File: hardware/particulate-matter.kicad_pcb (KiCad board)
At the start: 2 copper layers, 70 x 40 mm, 30 parts, among them P1 CON-SENSOR2, P2 BOOT, P3 DEBUG, U1 XMC1XXX48, U2 DRILL, U3 DRILL, U4 DRILL, U5 DRILL, U6 PMS7003, X1 16MHz

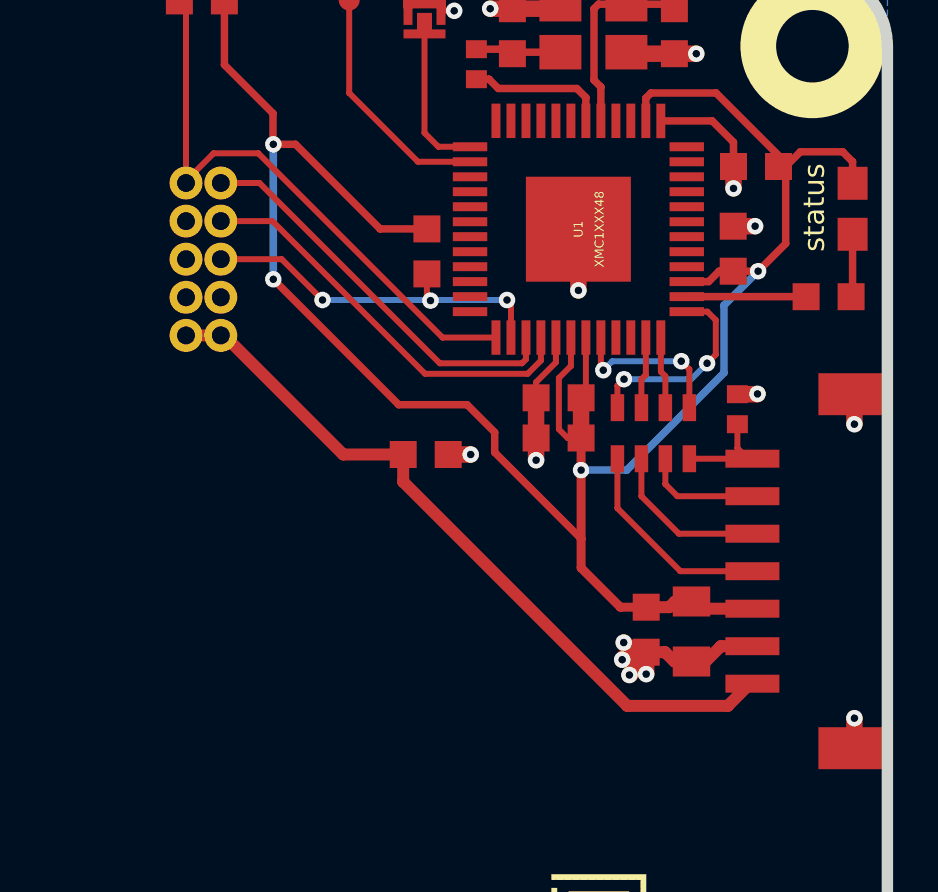
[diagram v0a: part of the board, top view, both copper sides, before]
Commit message: Add resistors for TX/RX and another capacitor for the PMS Sensor
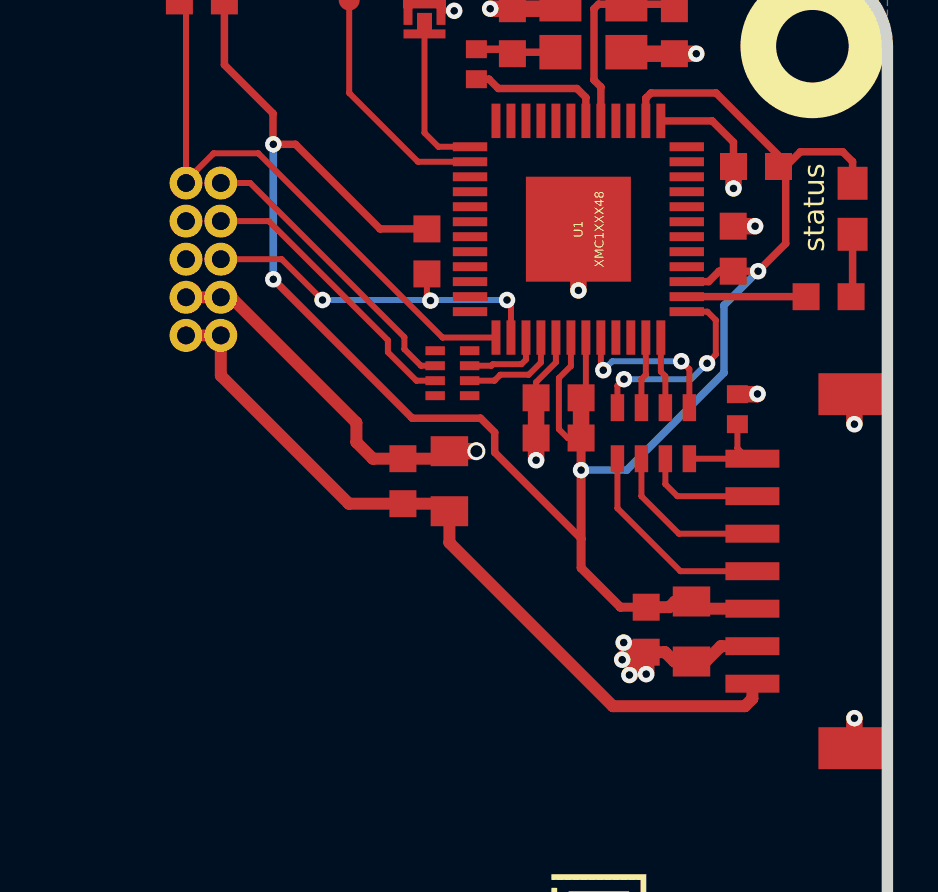
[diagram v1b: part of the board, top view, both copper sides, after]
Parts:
- added C11: 10uF, kicad-libraries:C0805, F.Cu at (156.2, 82.0)
- added RP2: 100, 4X0402, F.Cu at (156.3, 78.4)
- C1: value 1uF -> 10uF
- moved C10 1.17 mm to (154.7, 82.0), turned to 90 degrees
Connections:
- U6 pad 7: PMS_RX -> Net-(RP2-Pad3)
- U6 pad 9: PMS_TX -> Net-(RP2-Pad2)
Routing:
- net GND: track 29.2 -> 40.9 mm
- net PMS_TX: track 13.4 -> 2.70 mm
- net PMS_RX: track 13.7 -> 3.46 mm
- net Net-(RP2-Pad2): track 0.00 -> 9.90 mm
- net Net-(RP2-Pad3): track 0.00 -> 9.58 mm
- net +5V: track 24.8 -> 26.2 mm

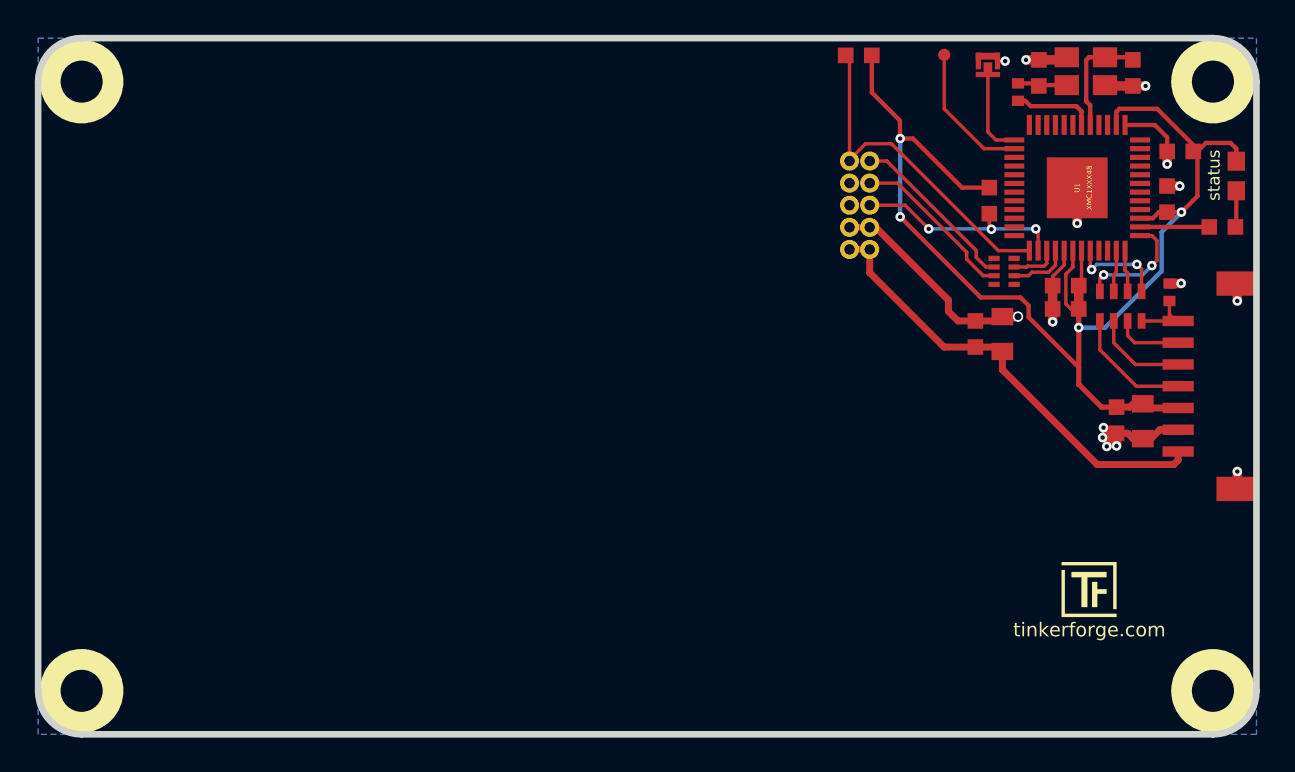
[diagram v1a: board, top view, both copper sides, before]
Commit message: add fiducial marks
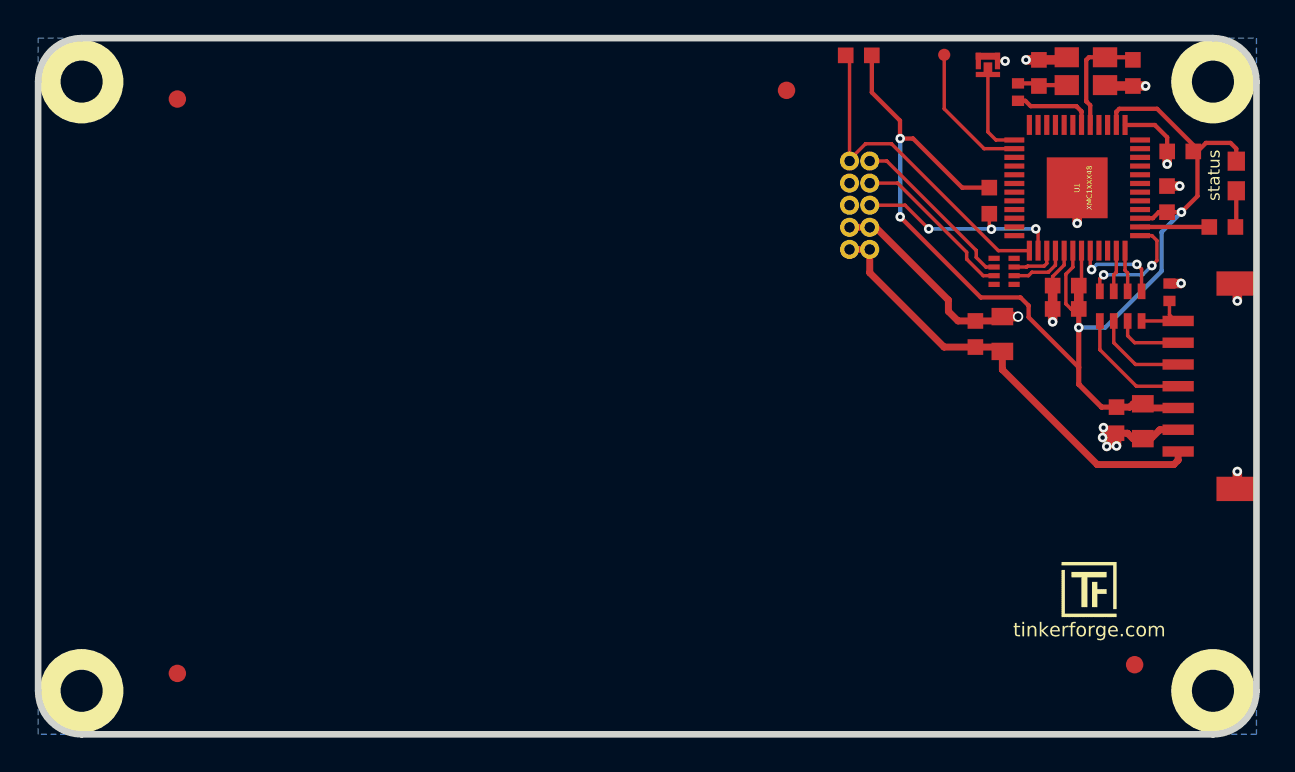
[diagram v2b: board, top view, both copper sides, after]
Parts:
- added Fiducial_Mark: VAL**, kicad-libraries:Fiducial_Mark, F.Cu at (163.8, 101.0)
- added Fiducial_Mark: VAL**, kicad-libraries:Fiducial_Mark, F.Cu at (108.8, 101.5)
- added Fiducial_Mark: VAL**, kicad-libraries:Fiducial_Mark, F.Cu at (108.8, 68.5)
- added Fiducial_Mark: VAL**, kicad-libraries:Fiducial_Mark, F.Cu at (143.8, 68.0)
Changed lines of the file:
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@@
-(kicad_pcb (version 4) (host pcbnew 4.0.2+dfsg1-stable)
+(kicad_pcb (version 4) (host pcbnew 4.0.7-e2-6376~58~ubuntu17.04.1)
   (general
     (links 67)
     (no_connects 0)
-    (area 100.609499 64.809499 170.990501 105.190501)
+    (area 14.621426 64.145139 171.654861 193.825)
     (thickness 1.6)
     (drawings 11)
     (tracks 241)
     (zones 0)
-    (modules 32)
+    (modules 36)
     (nets 60)
   )
@@
   )
   (setup
-    (last_trace_width 0.4)
+    (last_trace_width 0.25)
     (user_trace_width 0.2)
     (user_trace_width 0.25)
@@
     )
   )
+  (module kicad-libraries:Fiducial_Mark (layer F.Cu)
+    (at 163.8 101)
+    (attr smd)
+    (fp_text reference Fiducial_Mark (at 0 0) (layer F.SilkS) hide
+      (effects (font (size 0.127 0.127) (thickness 0.03302)))
+    )
+    (fp_text value VAL** (at 0 -0.29972) (layer F.SilkS) hide
+      (effects (font (size 0.127 0.127) (thickness 0.03302)))
+    )
+    (fp_circle (center 0 0) (end 1.15062 0) (layer Dwgs.User) (width 0.01016))
+    (pad 1 smd circle (at 0 0) (size 1.00076 1.00076) (layers F.Cu F.Paste F.Mask)
+      (clearance 0.65024))
+  )
+  (module kicad-libraries:Fiducial_Mark (layer F.Cu)
+    (at 108.8 101.5)
+    (attr smd)
+    (fp_text reference Fiducial_Mark (at 0 0) (layer F.SilkS) hide
+      (effects (font (size 0.127 0.127) (thickness 0.03302)))
+    )
+    (fp_text value VAL** (at 0 -0.29972) (layer F.SilkS) hide
+      (effects (font (size 0.127 0.127) (thickness 0.03302)))
+    )
+    (fp_circle (center 0 0) (end 1.15062 0) (layer Dwgs.User) (width 0.01016))
+    (pad 1 smd circle (at 0 0) (size 1.00076 1.00076) (layers F.Cu F.Paste F.Mask)
+      (clearance 0.65024))
+  )
+  (module kicad-libraries:Fiducial_Mark (layer F.Cu)
+    (at 108.8 68.5)
+    (attr smd)
+    (fp_text reference Fiducial_Mark (at 0 0) (layer F.SilkS) hide
+      (effects (font (size 0.127 0.127) (thickness 0.03302)))
+    )
+    (fp_text value VAL** (at 0 -0.29972) (layer F.SilkS) hide
+      (effects (font (size 0.127 0.127) (thickness 0.03302)))
+    )
+    (fp_circle (center 0 0) (end 1.15062 0) (layer Dwgs.User) (width 0.01016))
+    (pad 1 smd circle (at 0 0) (size 1.00076 1.00076) (layers F.Cu F.Paste F.Mask)
+      (clearance 0.65024))
+  )
+  (module kicad-libraries:Fiducial_Mark (layer F.Cu)
+    (at 143.8 68)
+    (attr smd)
+    (fp_text reference Fiducial_Mark (at 0 0) (layer F.SilkS) hide
+      (effects (font (size 0.127 0.127) (thickness 0.03302)))
+    )
+    (fp_text value VAL** (at 0 -0.29972) (layer F.SilkS) hide
+      (effects (font (size 0.127 0.127) (thickness 0.03302)))
+    )
+    (fp_circle (center 0 0) (end 1.15062 0) (layer Dwgs.User) (width 0.01016))
+    (pad 1 smd circle (at 0 0) (size 1.00076 1.00076) (layers F.Cu F.Paste F.Mask)
+      (clearance 0.65024))
+  )
   (gr_text tinkerforge.com (at 161.2 99) (layer F.SilkS)

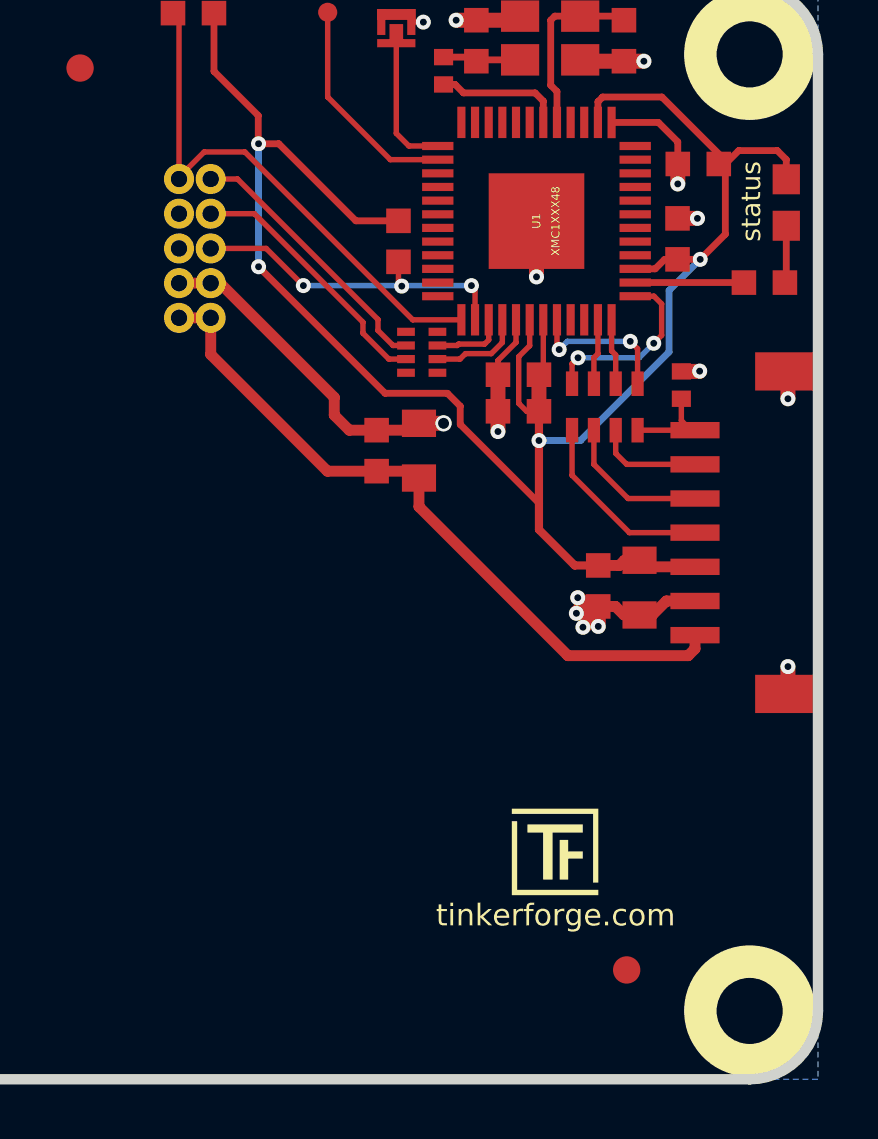
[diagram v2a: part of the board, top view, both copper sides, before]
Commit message: fix pms footprint, add title
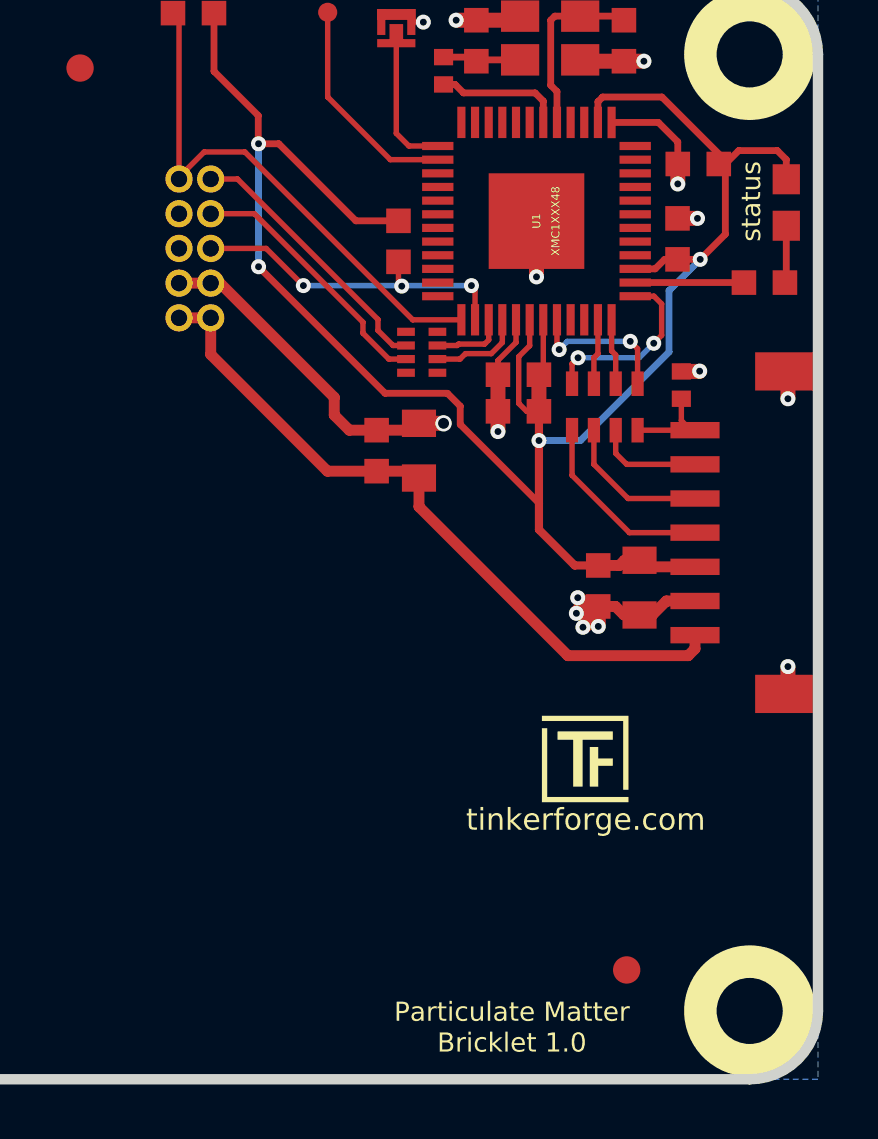
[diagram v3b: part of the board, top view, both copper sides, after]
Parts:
- moved G*** 3.57 mm to (160.7, 91.7)
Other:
- board text added: "Particulate Matter Bricklet 1.0"
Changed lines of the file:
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@@
     (area 14.621426 64.145139 171.654861 193.825)
     (thickness 1.6)
-    (drawings 11)
+    (drawings 12)
     (tracks 241)
     (zones 0)
@@
     (user_trace_width 0.55)
     (trace_clearance 0.14986)
-    (zone_clearance 0.508)
+    (zone_clearance 0.2)
     (zone_45_only no)
     (trace_min 0.2)
@@
       (clearance 0.89916))
   )
-  (module kicad-libraries:PMS7003 (layer F.Cu)
-    (at 130.3 85.1)
-    (fp_text reference U6 (at 0 0.5) (layer F.Fab)
-      (effects (font (size 0.5 0.5) (thickness 0.125)))
-    )
-    (fp_text value PMS7003 (at 0 -0.5) (layer F.Fab)
-      (effects (font (size 0.5 0.5) (thickness 0.125)))
-    )
-    (fp_line (start 20.7 -5.5) (end 20.7 -15.5) (layer F.Fab) (width 0.1))
-    (fp_line (start 20.7 -15.5) (end 14.7 -15.5) (layer F.Fab) (width 0.1))
-    (fp_line (start 14.7 -15.5) (end 14.7 -5.5) (layer F.Fab) (width 0.1))
-    (fp_line (start 14.7 -5.5) (end 20.7 -5.5) (layer F.Fab) (width 0.1))
-    (fp_line (start 23.55 -18.35) (end 23.55 18.35) (layer F.Fab) (width 0.1))
-    (fp_line (start 23.55 18.35) (end -23.55 18.35) (layer F.Fab) (width 0.1))
-    (fp_line (start -23.55 18.35) (end -23.55 -18.35) (layer F.Fab) (width 0.1))
-    (fp_line (start -23.55 -18.35) (end 23.55 -18.35) (layer F.Fab) (width 0.1))
-    (pad 9 thru_hole circle (at 18.28 -13.04) (size 1.1 1.1) (drill 0.6) (layers *.Cu *.Mask F.SilkS)
-      (net 58 "Net-(RP2-Pad2)"))
-    (pad 7 thru_hole circle (at 18.28 -11.77) (size 1.1 1.1) (drill 0.6) (layers *.Cu *.Mask F.SilkS)
-      (net 59 "Net-(RP2-Pad3)"))
-    (pad 5 thru_hole circle (at 18.28 -10.5) (size 1.1 1.1) (drill 0.6) (layers *.Cu *.Mask F.SilkS)
-      (net 14 PMS_RESET))
-    (pad 3 thru_hole circle (at 18.28 -9.23) (size 1.1 1.1) (drill 0.6) (layers *.Cu *.Mask F.SilkS)
-      (net 1 GND))
-    (pad 1 thru_hole circle (at 18.28 -7.96) (size 1.1 1.1) (drill 0.6) (layers *.Cu *.Mask F.SilkS)
-      (net 6 +5V))
-    (pad 2 thru_hole circle (at 17.12 -7.96) (size 1.1 1.1) (drill 0.6) (layers *.Cu *.Mask F.SilkS)
-      (net 6 +5V))
-    (pad 4 thru_hole circle (at 17.12 -9.23) (size 1.1 1.1) (drill 0.6) (layers *.Cu *.Mask F.SilkS)
-      (net 1 GND))
-    (pad 6 thru_hole circle (at 17.12 -10.5) (size 1.1 1.1) (drill 0.6) (layers *.Cu *.Mask F.SilkS)
-      (net 50 "Net-(U6-Pad6)"))
-    (pad 8 thru_hole circle (at 17.12 -11.77) (size 1.1 1.1) (drill 0.6) (layers *.Cu *.Mask F.SilkS)
-      (net 51 "Net-(U6-Pad8)"))
-    (pad 10 thru_hole circle (at 17.12 -13.04) (size 1.1 1.1) (drill 0.6) (layers *.Cu *.Mask F.SilkS)
-      (net 13 PMS_SET))
-  )
   (module kicad-libraries:C0402F (layer F.Cu)
     (at 165.8 79.6 90)
@@
   )
   (module kicad-libraries:Logo_31x31 (layer F.Cu)
-    (at 159.6 95.1)
+    (at 160.7 91.7)
     (fp_text reference G*** (at 1.34874 2.97434) (layer F.SilkS) hide
       (effects (font (size 0.29972 0.29972) (thickness 0.0762)))
@@
       (clearance 0.65024))
   )
-  (gr_text tinkerforge.com (at 161.2 99) (layer F.SilkS)
+  (module kicad-libraries:PMS7003 (layer F.Cu)
+    (at 130.3 85.1)
+    (fp_text reference U6 (at 0 0.5) (layer F.Fab)
+      (effects (font (size 0.5 0.5) (thickness 0.125)))
+    )
+    (fp_text value PMS7003 (at 0 -0.5) (layer F.Fab)
+      (effects (font (size 0.5 0.5) (thickness 0.125)))
+    )
+    (fp_line (start 20.7 -5.5) (end 20.7 -15.5) (layer F.Fab) (width 0.1))
+    (fp_line (start 20.7 -15.5) (end 14.7 -15.5) (layer F.Fab) (width 0.1))
+    (fp_line (start 14.7 -15.5) (end 14.7 -5.5) (layer F.Fab) (width 0.1))
+    (fp_line (start 14.7 -5.5) (end 20.7 -5.5) (layer F.Fab) (width 0.1))
+    (fp_line (start 23.55 -18.35) (end 23.55 18.35) (layer F.Fab) (width 0.1))
+    (fp_line (start 23.55 18.35) (end -23.55 18.35) (layer F.Fab) (width 0.1))
+    (fp_line (start -23.55 18.35) (end -23.55 -18.35) (layer F.Fab) (width 0.1))
+    (fp_line (start -23.55 -18.35) (end 23.55 -18.35) (layer F.Fab) (width 0.1))
+    (pad 9 thru_hole circle (at 18.28 -13.04) (size 1 1) (drill 0.6) (layers *.Cu *.Mask F.SilkS)
+      (net 58 "Net-(RP2-Pad2)"))
+    (pad 7 thru_hole circle (at 18.28 -11.77) (size 1 1) (drill 0.6) (layers *.Cu *.Mask F.SilkS)
+      (net 59 "Net-(RP2-Pad3)"))
+    (pad 5 thru_hole circle (at 18.28 -10.5) (size 1 1) (drill 0.6) (layers *.Cu *.Mask F.SilkS)
+      (net 14 PMS_RESET))
+    (pad 3 thru_hole circle (at 18.28 -9.23) (size 1 1) (drill 0.6) (layers *.Cu *.Mask F.SilkS)
+      (net 1 GND))
+    (pad 1 thru_hole circle (at 18.28 -7.96) (size 1 1) (drill 0.6) (layers *.Cu *.Mask F.SilkS)
+      (net 6 +5V))
+    (pad 2 thru_hole circle (at 17.12 -7.96) (size 1 1) (drill 0.6) (layers *.Cu *.Mask F.SilkS)
+      (net 6 +5V))
+    (pad 4 thru_hole circle (at 17.12 -9.23) (size 1 1) (drill 0.6) (layers *.Cu *.Mask F.SilkS)
+      (net 1 GND))
+    (pad 6 thru_hole circle (at 17.12 -10.5) (size 1 1) (drill 0.6) (layers *.Cu *.Mask F.SilkS)
+      (net 50 "Net-(U6-Pad6)"))
+    (pad 8 thru_hole circle (at 17.12 -11.77) (size 1 1) (drill 0.6) (layers *.Cu *.Mask F.SilkS)
+      (net 51 "Net-(U6-Pad8)"))
+    (pad 10 thru_hole circle (at 17.12 -13.04) (size 1 1) (drill 0.6) (layers *.Cu *.Mask F.SilkS)
+      (net 13 PMS_SET))
+  )
+  (gr_text "Particulate Matter\nBricklet 1.0" (at 159.6 103.1) (layer F.SilkS)
+    (effects (font (size 0.7 0.7) (thickness 0.15)))
+  )
+  (gr_text tinkerforge.com (at 162.3 95.5) (layer F.SilkS)
     (effects (font (size 0.8 0.8) (thickness 0.15)))
   )
@@
   (segment (start 155.09892 78.64892) (end 154.15 77.7) (width 0.2) (layer F.Cu) (net 59))
   (zone (net 1) (net_name GND) (layer B.Cu) (hatch edge 0.508)
-    (connect_pads yes (clearance 0.508))
-    (min_thickness 0.254)
+    (connect_pads yes (clearance 0.2))
+    (min_thickness 0.15)
     (fill yes (arc_segments 16) (thermal_gap 0.508) (thermal_bridge_width 0.508))
     (polygon
       (pts
-        (xy 170.8 105) (xy 100.8 105) (xy 100.8 65) (xy 170.8 65) (xy 170.8 105)
+        (xy 170.8 105) (xy 100.8 105) (xy 100.8 65) (xy 170.8 65)
       )
     )
